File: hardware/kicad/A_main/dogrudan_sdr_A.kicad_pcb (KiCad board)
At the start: 6 copper layers, 235 x 225 mm, 297 parts, among them J1 XT60, J10 JTAG 2x3, J20 SMA A1, J21 SMA B1, J22 SMA A2, J23 SMA B2, J30 SMA TX1, J31 SMA TX2, J32 SMA TX3, J33 SMA TX4, J40 HR911130A, J41 HR911130A, J60 GPS modul, J61 SMA 10MHz ref, J62 DAC modul, J63 C kartina, J64 UART 3.3V, J65 C kartina #2, J66 D kartina, Q1 DMP3098L, SW1 PROG, T1 ADT1-1WT+, T10 ADT1-1WT+, T11 ADT1-1WT+, T12 ADT1-1WT+, T13 ADT1-1WT+, T2 ADT1-1WT+, T3 ADT1-1WT+, T4 ADT1-1WT+, U1 TPS62130, U10 LFE5U-25F-7BG256I, U11 W25Q128JVSIQ, U15 ADCLK846BCPZ, U16 SN65LVDS2DBVR, U17 SN65LVDS2DBVR, U18 SN65LVDS2DBVR, U2 TPS62130, U20 AD9251BCPZ-80, U21 AD9251BCPZ-80, U3 TPS7A2033, U30 AD9767ASTZ, U31 AD9767ASTZ, U4 ADP150, U40 RTL8211FI-CG, U41 RTL8211FI-CG, U5 ADP150, U50 W9825G6KH-6I, U6 ADP150, U62 TLV3501AIDBVR, U7 ADP150, U8 ADP150, U9 ADP150, Y10 ABLNO-V-80.000MHZ, Y610 25MHz CL12pF, Y626 25MHz CL12pF

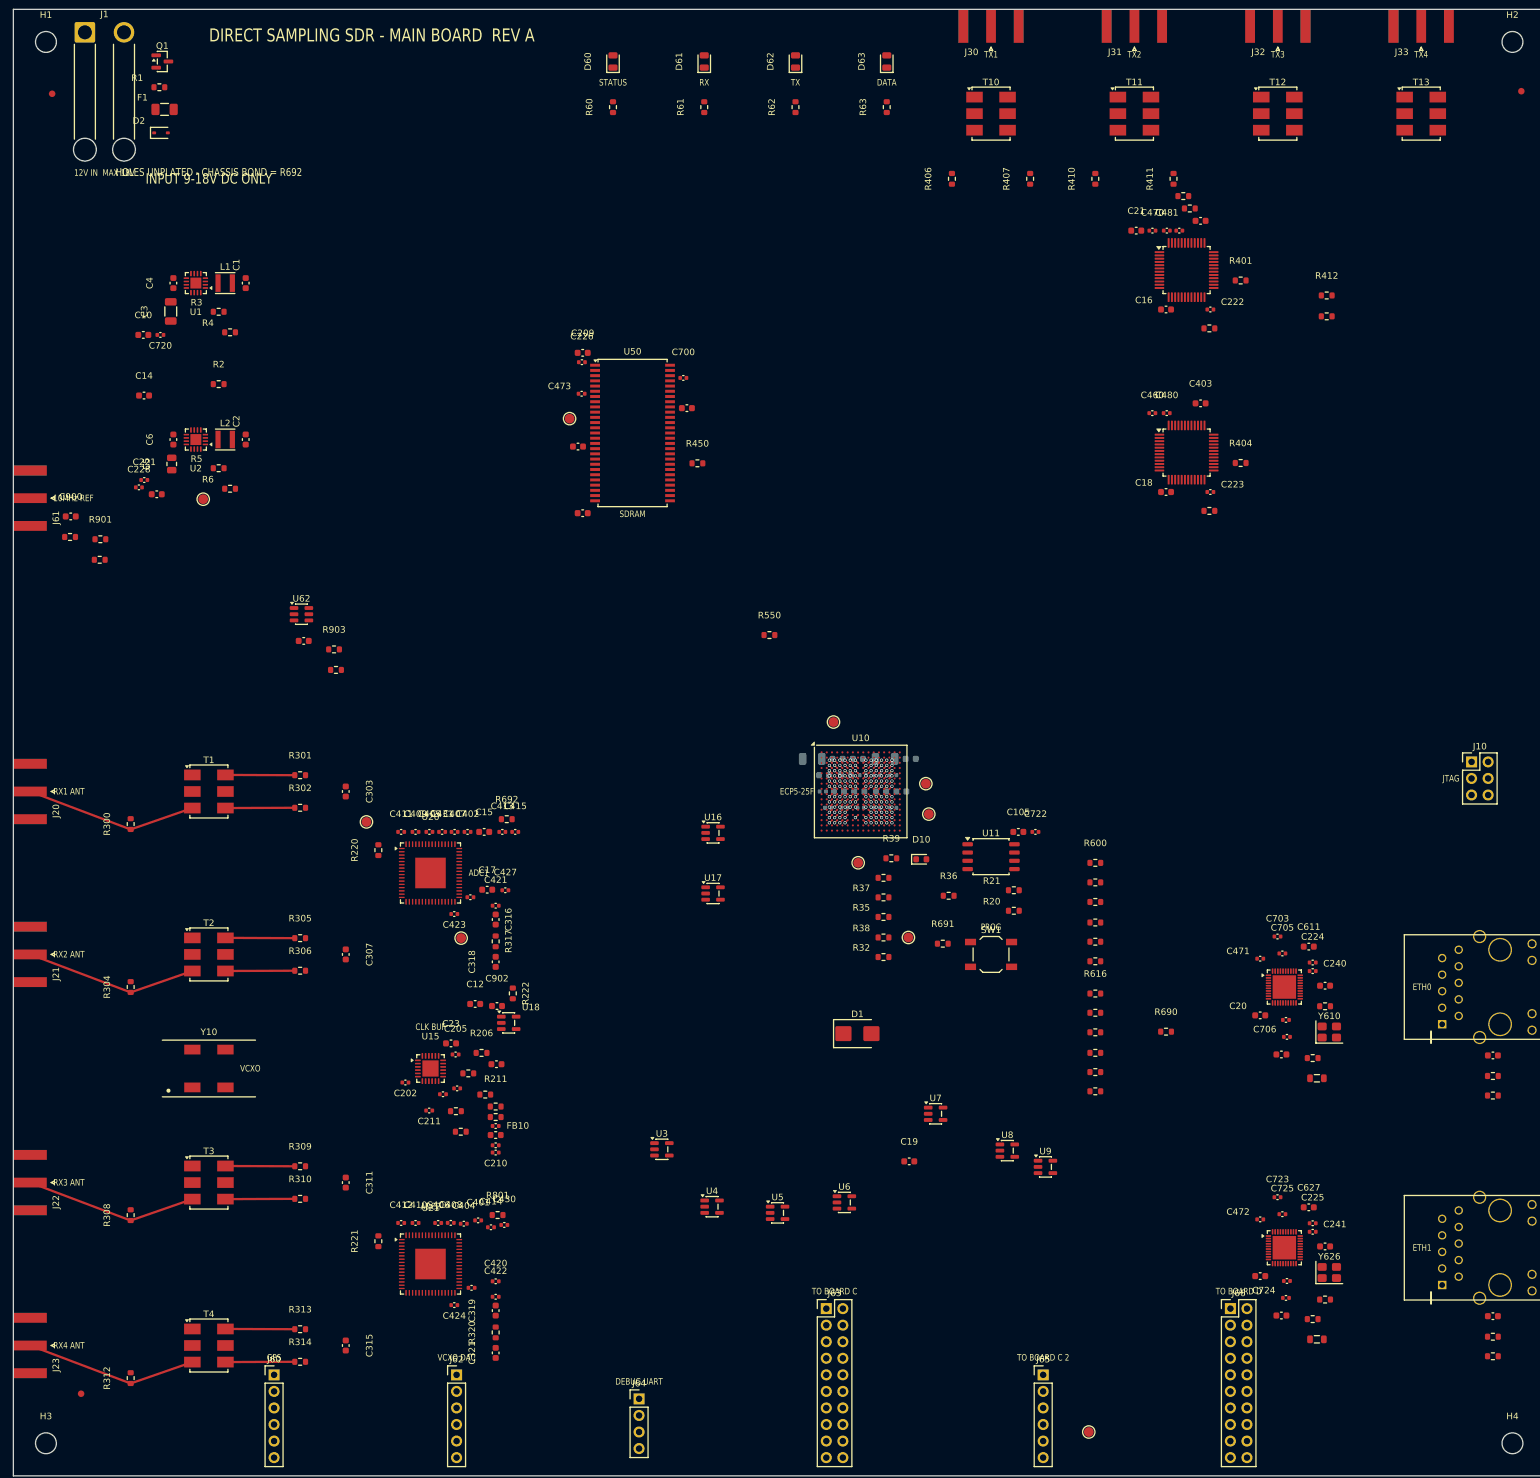
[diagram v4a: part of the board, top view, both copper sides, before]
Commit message: Move each decoupling capacitor to the pin it serves
The audit found 14 chips with no decoupling capacitor within 15 mm.
Across the boards the nearest capacitor to a supply rail was a median
7.5 mm on A and 6.3 mm on C, and 91 mm in the worst case. A capacitor
45 mm from its pin has about 45 nH of loop inductance, near 2.8 ohm at
10 MHz, where milliohms are necessary. It is on the schematic, it is
in the BOM, it is fitted, and it does nothing.

The pass that moves capacitors ran before the fallback placer, so a
chip with no explicit rule was not yet placed and never entered the
pool. The fallback then gave every spare capacitor to the chip with
the most pins on the rail, which is the FPGA on +3V3. Small parts got
none. The pass now runs last.

A count of missing parts was also wrong. Every pad on a rail was
counted as a supply pin, including logic inputs tied high: SRCLR on
the 74HC595, SLEEP on the DRV8833, P/S on the PE4312. Counting only
pins the netlist marks power_in, board C has 15 supply pins and 15
capacitors. Four capacitors are missing across all three boards, not
59. The AD8318 has three supply pins and had one capacitor; it now
has three. The ADCLK846 has six and had five.
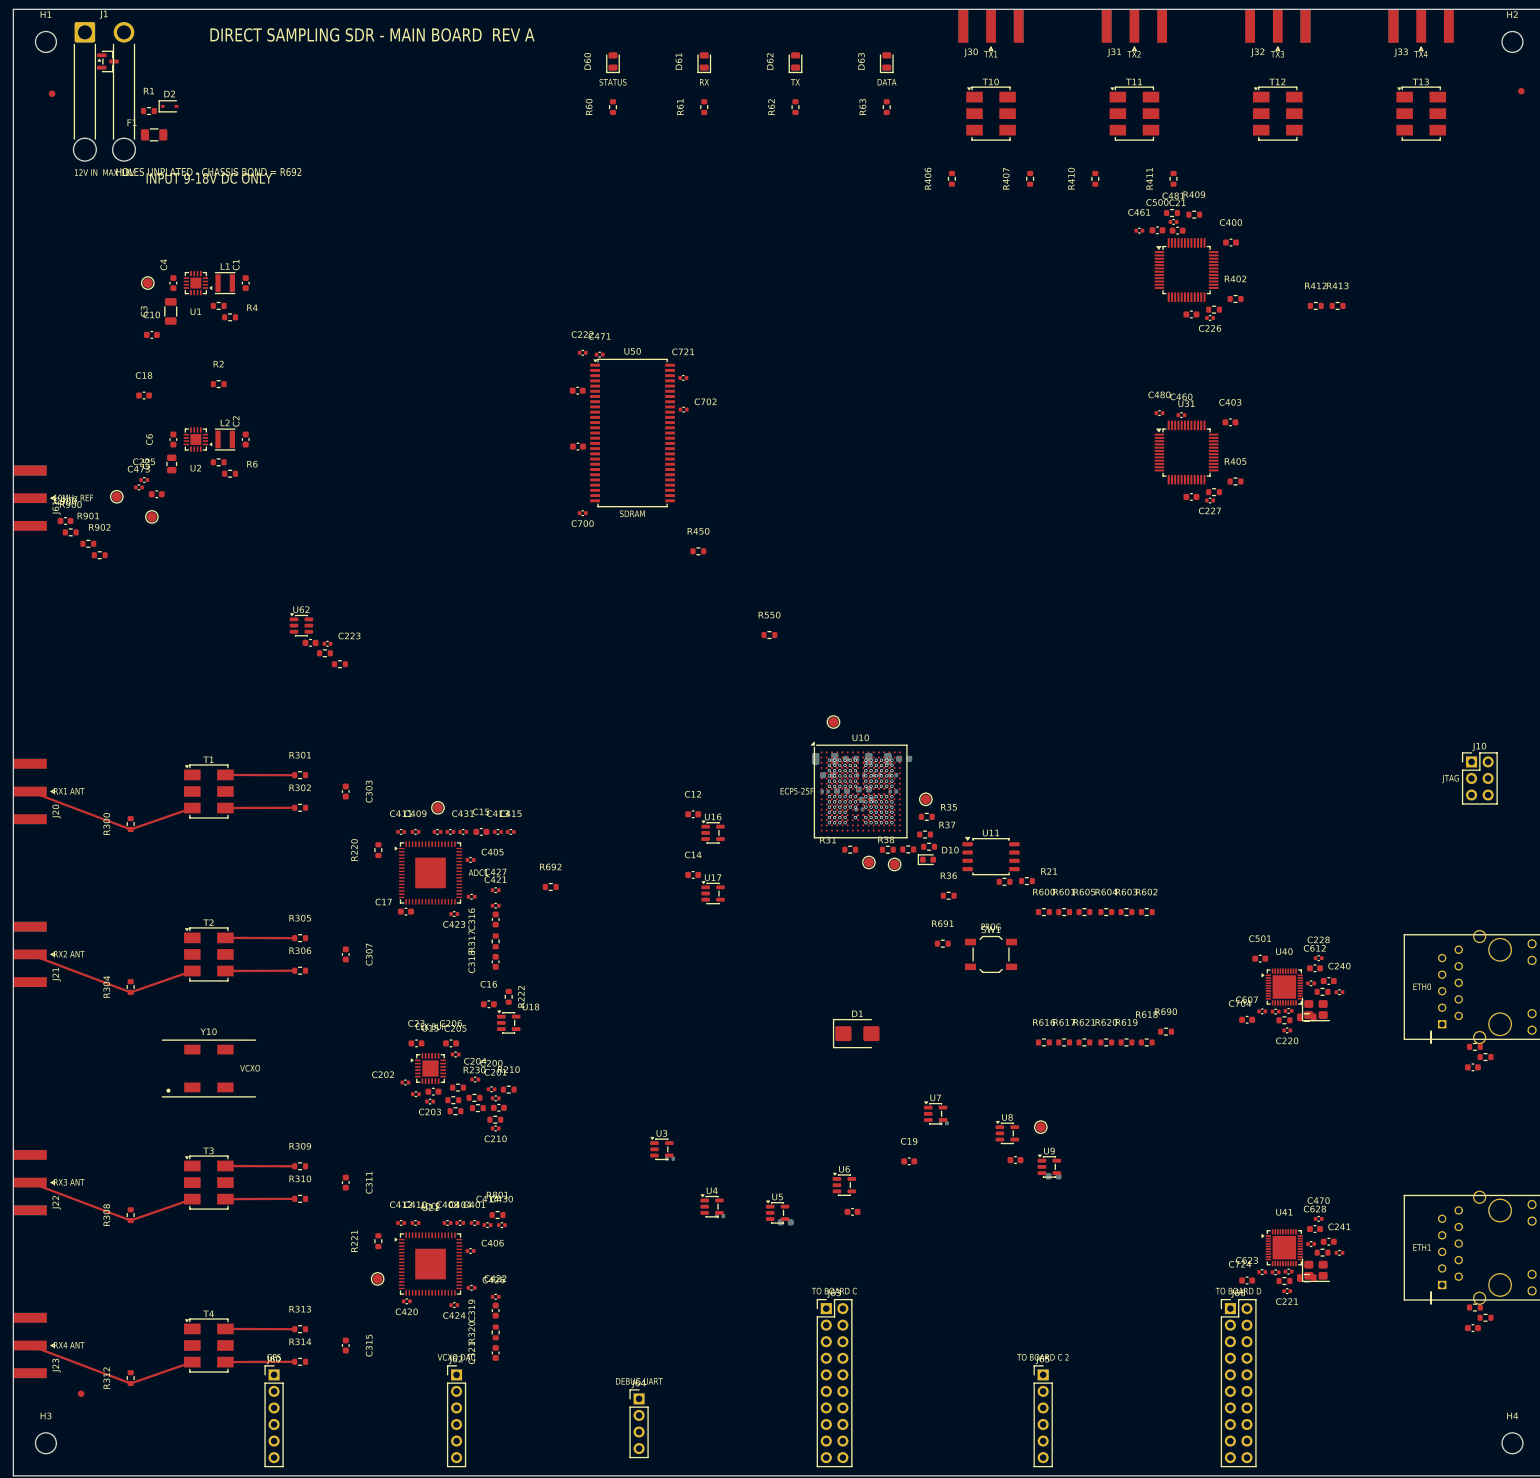
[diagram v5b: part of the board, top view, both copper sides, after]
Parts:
- removed C207, C209: 100nF, C_0603_1608Metric
- removed R206, R208: 100R, R_0603_1608Metric
- added C206: 10uF, C_0603_1608Metric, F.Cu at (67.2, 158.7)
- added C208: 100nF, C_0603_1608Metric, F.Cu at (180.7, 74.8)
- added R207: 100R, R_0603_1608Metric, F.Cu at (71.3, 168.6)
- added R209: 100R, R_0603_1608Metric, F.Cu at (68.2, 165.4)
- C220, C227, C500, C502, C702, C721: moved to F.Cu
- C224, C472, C720, C722, C902: moved to B.Cu
- moved TP6 227.9 mm to (20.6, 42.0)
- moved C221 215.0 mm to (195.4, 196.7)
- moved C225 212.5 mm to (20.1, 72.2)
- moved C228 194.9 mm to (200.3, 145.6)
- moved C18 157.5 mm to (20.1, 59.2)
- moved C470 153.8 mm to (200.3, 185.6)
- moved C16 148.9 mm to (73.0, 152.7)
- moved C720 148.6 mm to (100.8, 176.3)
- moved C223 137.5 mm to (48.2, 97.3)
- moved C471 137.3 mm to (90.0, 53.0)
- moved C501 130.9 mm to (191.3, 145.7)
- moved C14 111.8 mm to (104.3, 132.8)
- moved C20 108.1 mm to (180.7, 46.8)
- moved C500 99.0 mm to (175.5, 33.9)
- moved C226 96.6 mm to (183.6, 47.4)
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
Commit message: Do not count a bulk capacitor as decoupling
The placement pass accepted any capacitor on the rail as sufficient.
On board A the flash memory had 10 uF at 5.5 mm and 47 uF at 16.3 mm,
so the pass was satisfied. Both are bulk. The nearest 100 nF was
17.0 mm away, and at that distance the loop inductance removes the
reason to fit it.

The audit tool already used a 10 uF ceiling for this. The placer did
not, so the two disagreed, and the placer was wrong.

The pass now treats only capacitors of 1 uF and below as decoupling,
both when it asks whether a pin is served and when it selects one to
move. It also searches a ring around the pin for free space instead
of using a fixed offset.

Findings fall from 14 to 4. Board A is clean.

Also: build.sh never ran bom.py, so BOM_*.csv were hand-made files
that no step regenerated and the BOM no longer matched the schematic.
Each board's build now writes its own.
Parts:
- moved TP5 217.4 mm to (194.0, 199.4)
- moved TP10 83.6 mm to (44.6, 89.6)
- moved C22 69.4 mm to (127.5, 117.5)
- moved TP7 66.7 mm to (80.1, 150.5)
- moved C13 65.6 mm to (159.0, 173.6)
- moved C105 64.1 mm to (155.5, 126.2)
- moved C472 61.5 mm to (116.1, 180.9)
- moved C701 51.9 mm to (132.9, 120.0)
- moved C502 38.6 mm to (191.3, 185.7)
- moved C902 34.5 mm to (149.6, 171.1)
- moved TP1 22.1 mm to (36.5, 62.0)
- moved TP3 15.0 mm to (68.7, 202.5)
- moved TP2 14.3 mm to (77.4, 129.9)
- moved C420 14.0 mm to (74.0, 195.1)
- moved C17 12.9 mm to (72.7, 135.1)
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
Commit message: Let the placer, not the separator, own the capacitor position
Placing a capacitor beside its supply pin and then resolving overlaps
moves it away again. On board C the pass put a 100 nF 4.7 mm from the
attenuator's pin, the separator cleared 191 overlaps, and the
capacitor finished 17.9 mm away.

The pass now runs after separation and searches for free space around
the pin itself, so it does not need the separator afterwards. It
moves 21 capacitors on A, 26 on C and 12 on D.

Measured at the supply pin, the median distance is 2.8 mm on A,
5.4 mm on C and 4.6 mm on D. Board C's worst supply pin improves from
98.5 mm to 8.9 mm. Findings fall from 14 to 1.
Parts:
- moved TP6 227.2 mm to (165.0, 217.1)
- moved TP5 219.3 mm to (18.1, 68.5)
- moved TP4 62.1 mm to (140.0, 119.6)
- moved C701 46.3 mm to (140.3, 165.7)
- moved C502 43.9 mm to (150.0, 170.8)
- moved C902 25.7 mm to (125.0, 178.8)
- moved TP2 12.2 mm to (67.7, 122.5)
- moved C423 12.1 mm to (56.2, 134.7)
- moved C424 12.1 mm to (56.2, 194.7)
- moved TP3 12.0 mm to (72.7, 191.2)
- moved C240 10.7 mm to (194.8, 142.6)
- moved C241 10.7 mm to (194.8, 182.6)
- moved C405 8.97 mm to (63.8, 126.2)
- moved C407 7.83 mm to (72.0, 129.8)
- moved C406 7.80 mm to (65.2, 186.2)
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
